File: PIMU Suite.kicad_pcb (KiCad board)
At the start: 2 copper layers, 93 x 69 mm, 23 parts, among them U2 MICROSD_SPI_OR_SDIO_CARD

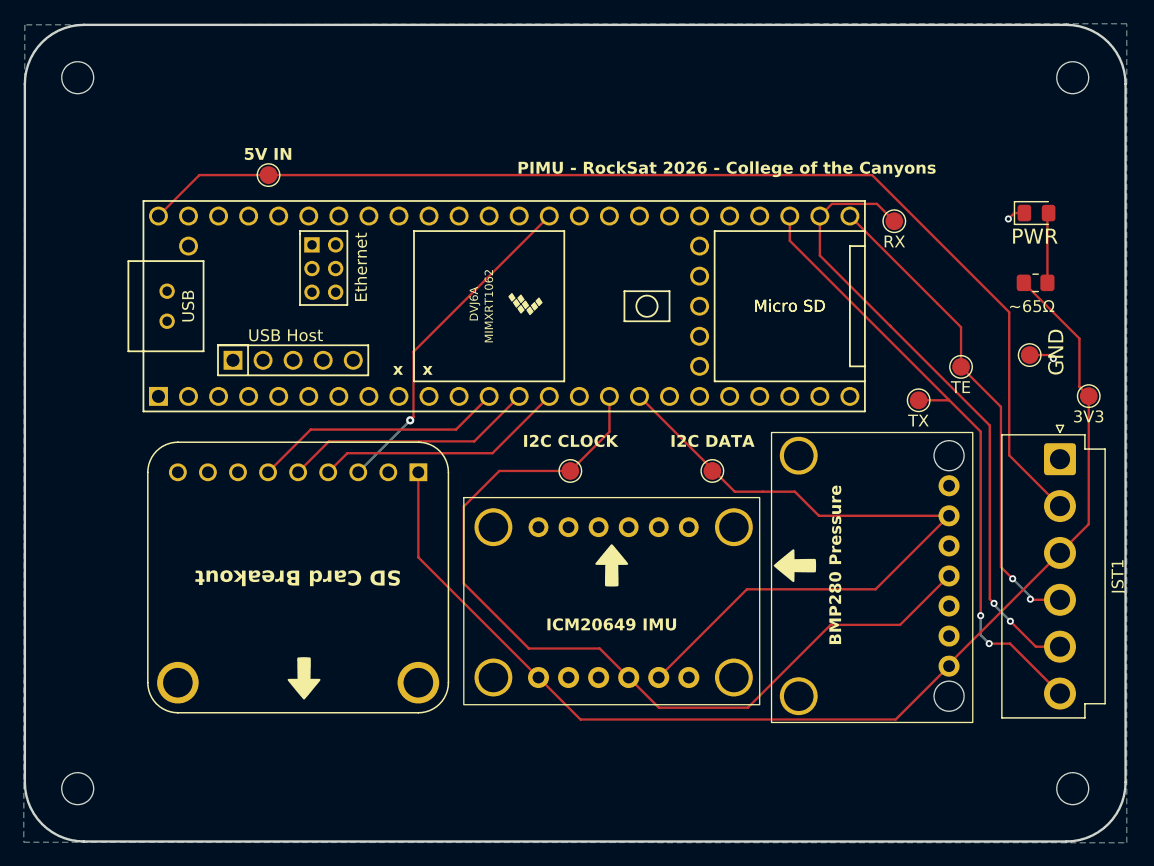
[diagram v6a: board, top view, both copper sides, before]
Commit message: USB headers + silkscreen
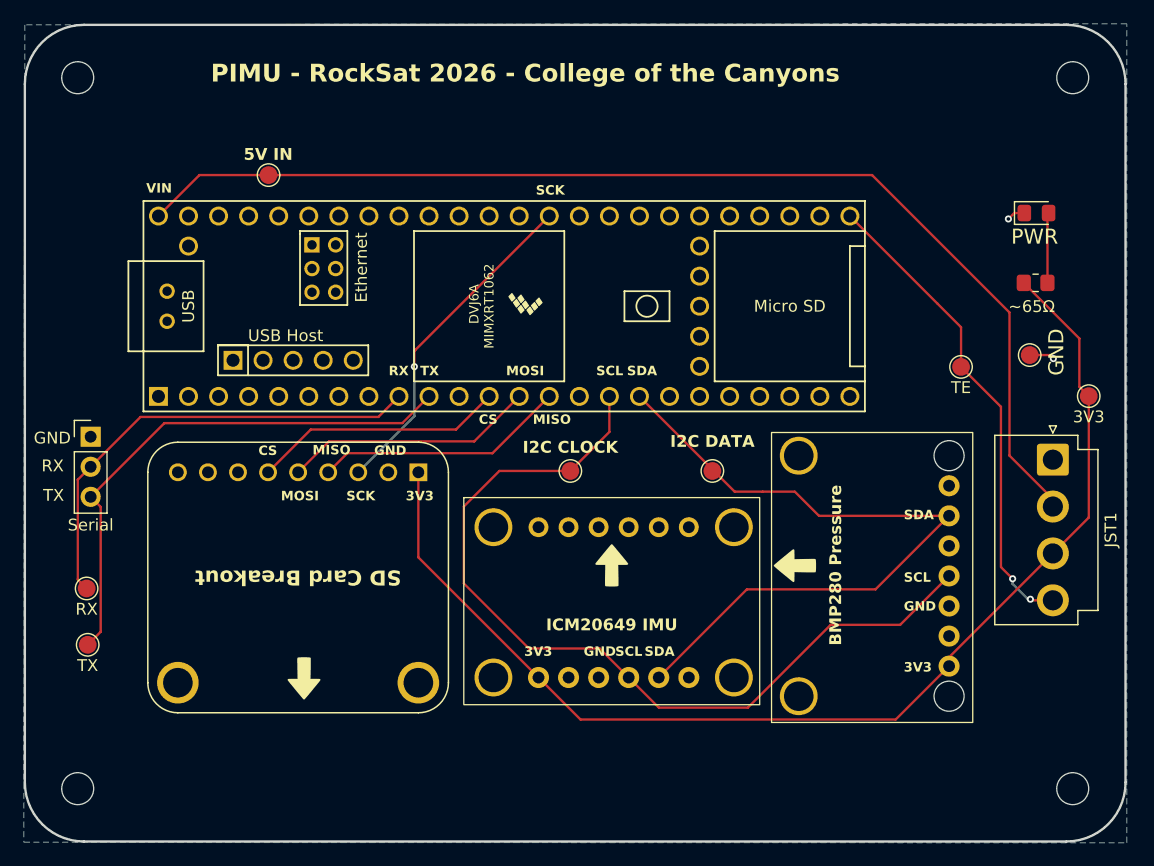
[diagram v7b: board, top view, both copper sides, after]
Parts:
- added G***: LOGO, LOGO, B.Cu at (181.0, 87.4)
- added HEADER1: Serial, Connector_PinHeader_2.54mm:PinHeader_1x03_P2.54mm_Vertical, F.Cu at (105.6, 101.8)
- JST1: value JST_VH_B6P-VH-B -> JST_VH_B4P-VH-B; footprint Connector_JST:JST_VH_B6P-VH-B_1x06_P3.96mm_Vertical -> Connector_JST:JST_VH_B4P-VH-B_1x04_P3.96mm_Vertical
- moved TP8 75.0 mm to (105.2, 114.6)
- moved TP7 73.2 mm to (105.3, 119.4)
- moved JST1 0.60 mm to (186.9, 103.7)
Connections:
- TEENSY1 pad 10: unconnected-(TEENSY1-8_TX2_IN1-Pad10) -> /UART_FROM_TEENSY
- TEENSY1 pad 26: /UART_TO_TEENSY -> unconnected-(TEENSY1-34_RX8-Pad26)
- TEENSY1 pad 27: /UART_FROM_TEENSY -> unconnected-(TEENSY1-35_TX8-Pad27)
- TEENSY1 pad 9: unconnected-(TEENSY1-7_RX2_OUT1A-Pad9) -> /UART_TO_TEENSY
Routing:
- net /UART_TO_TEENSY: track 53.4 -> 39.6 mm, vias 2 -> 0
- net /UART_FROM_TEENSY: track 53.4 -> 45.4 mm, vias 2 -> 0
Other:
- board text added: "3V3"
- board text added: "CS"
- board text added: "GND"
- board text added: "MISO"
- board text added: "MOSI"
- board text added: "RX"
- board text added: "SCK"
- board text added: "SCL"
- board text added: "SDA"
- board text added: "TX"
- board text added: "Two roads diverged in a wood, and I- I took the one less traveled by, And that has made all the difference. ~ Robert Frost"
- board text added: "VIN"
- board text removed: "Made with <3"
- board text removed: "Micro SD"
- board text removed: "x"
